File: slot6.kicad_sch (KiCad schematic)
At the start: 1 part

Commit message: board layout
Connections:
- net AD1: now also PL7.a3 (Pin_a3); no longer PL7.b3 (Pin_b3)
- net Chroma: now also PL7.a2 (Pin_a2); no longer PL7.b2 (Pin_b2)
- net GND: now also PL7.b3 (Pin_b3); no longer PL7.a3 (Pin_a3)
- net Luma: now also PL7.b2 (Pin_b2); no longer PL7.a2 (Pin_a2)
- net VCLK: now reaches PL7.a38 (Pin_a38)
- net ESND: now reaches PL7.b10 (Pin_b10)
- no-connect marks 1 -> 0

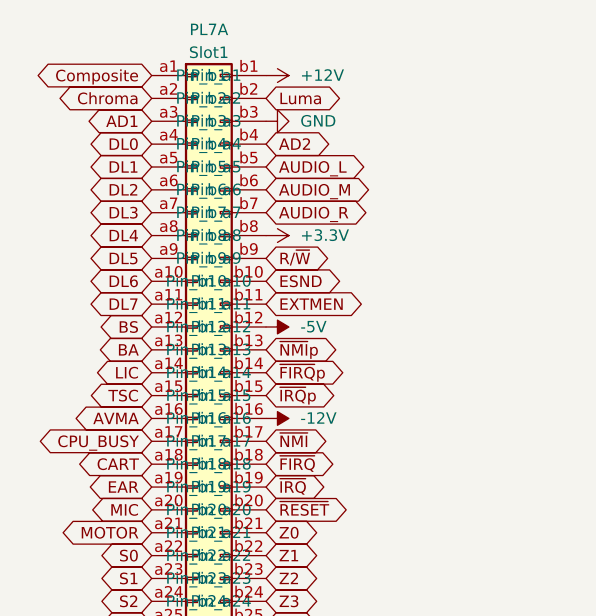
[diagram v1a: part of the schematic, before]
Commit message: revise bus tracing
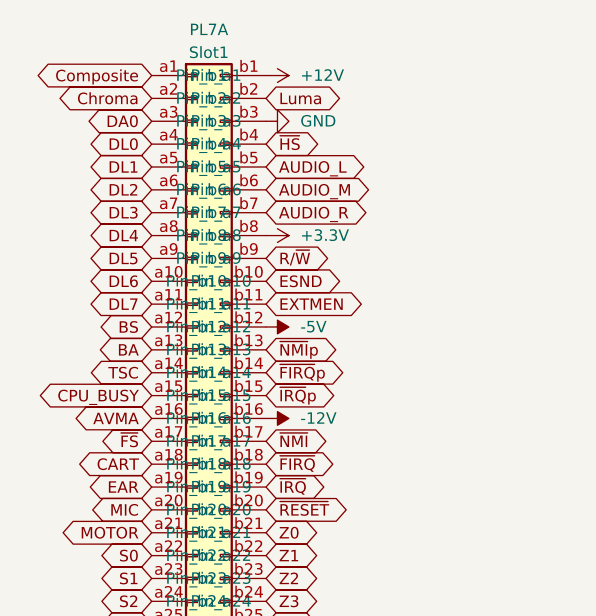
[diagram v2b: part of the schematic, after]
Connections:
- net LIC is gone; now on net TSC: PL7.a14 (Pin_a14)
- net CPU_BUSY: now also PL7.a15 (Pin_a15); no longer PL7.a17 (Pin_a17)
- net TSC: no longer PL7.a15 (Pin_a15)
- net AD1 renamed DA0
- net AD2 renamed ~{HS}
- new net ~{FS}: PL7.a17 (Pin_a17)
